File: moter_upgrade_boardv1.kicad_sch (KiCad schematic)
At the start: 41 parts, among them J10 Conn_01x03_Socket, J12 Conn_01x03_Socket, J2 USB_C_Receptacle_USB2.0_16P, J4 Conn_01x03_Socket, J5 Conn_01x02_Socket, J6 Conn_ST_STDC14, J7 Conn_01x02_Socket, J9 Conn_01x03_Socket, SW1 SW_Wuerth_450301014042, SW2 SW_Push, U1 BD33FC0FP, U2 STM32F446RETx, U3 MCP2562-E-P

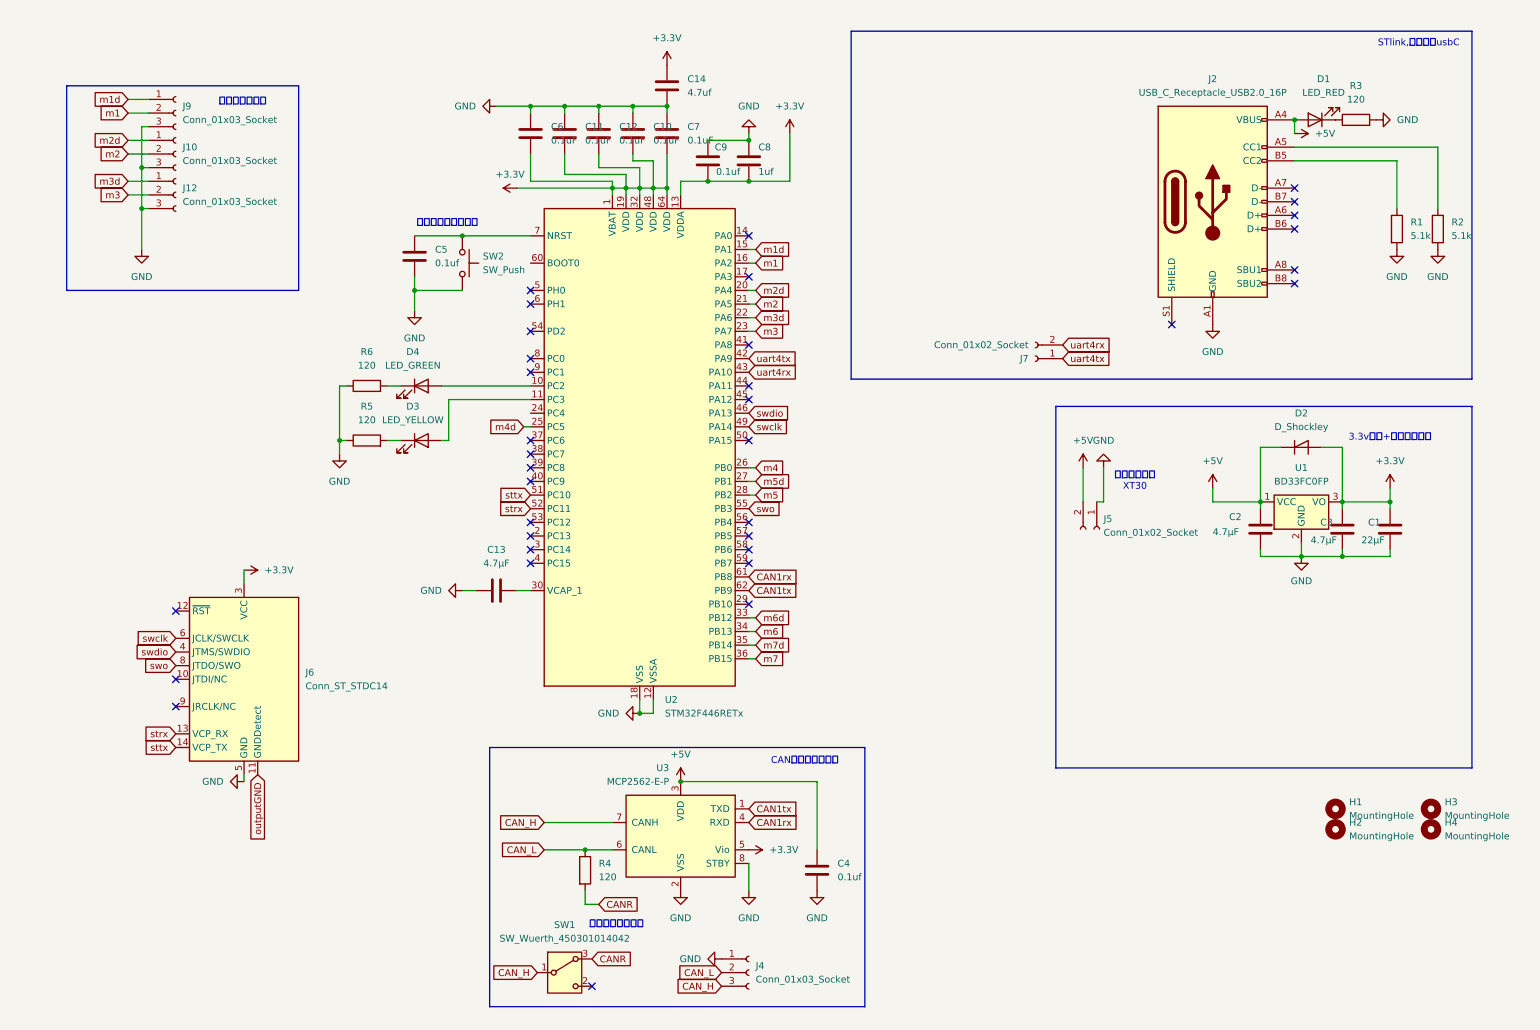
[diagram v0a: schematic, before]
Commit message: 絶縁回路の作成
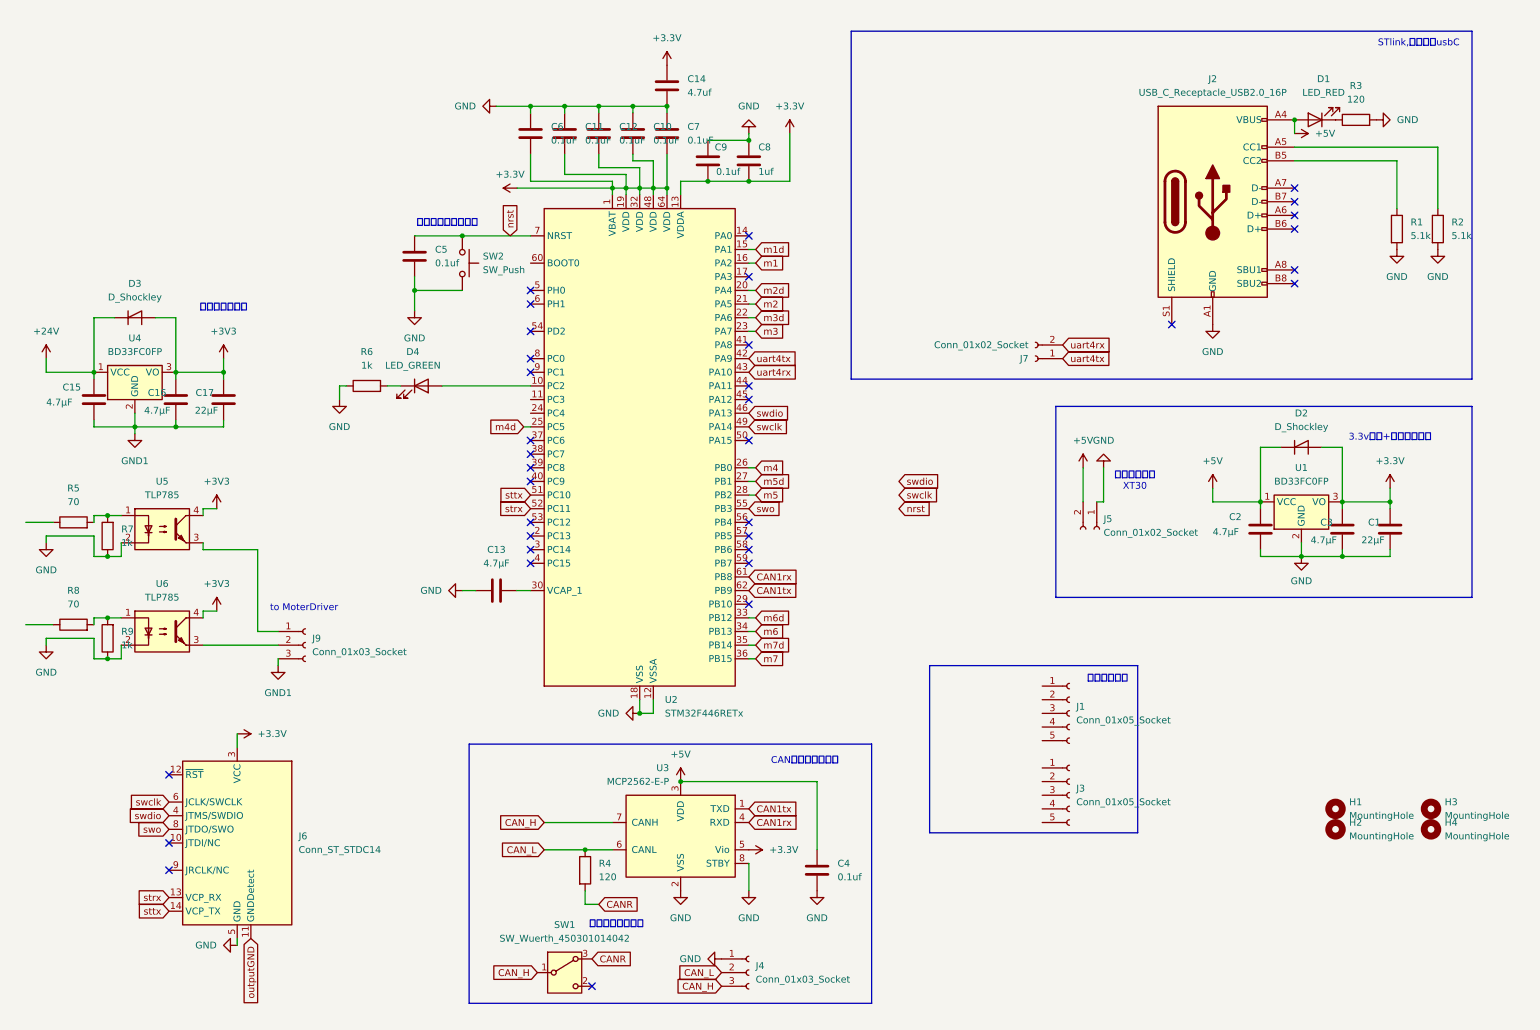
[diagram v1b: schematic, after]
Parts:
- removed D3: LED_YELLOW, Diode_SMD:D_0805_2012Metric_Pad1.15x1.40mm_HandSolder, symbol Device:LED
- removed J10, J12: Conn_01x03_Socket, Connector_JST:JST_XH_S3B-XH-A-1_1x03_P2.50mm_Horizontal, symbol Connector:Conn_01x03_Socket
- added C15, C16: 4.7μF, Capacitor_SMD:C_0805_2012Metric_Pad1.18x1.45mm_HandSolder, symbol Device:C
- added C17: 22μF, Capacitor_SMD:C_0805_2012Metric_Pad1.18x1.45mm_HandSolder, symbol Device:C
- added D3: D_Shockley, Diode_SMD:D_SOD-323_HandSoldering, symbol Device:D_Shockley
- added J1, J3: Conn_01x05_Socket, symbol Connector:Conn_01x05_Socket
- added R7, R9: 1k, Resistor_THT:R_Axial_DIN0207_L6.3mm_D2.5mm_P7.62mm_Horizontal, symbol Device:R
- added R8: 70, Resistor_THT:R_Axial_DIN0207_L6.3mm_D2.5mm_P7.62mm_Horizontal, symbol Device:R
- added U4: BD33FC0FP, Package_TO_SOT_SMD:TO-252-2, symbol Regulator_Linear:BD33FC0FP
- added U5, U6: TLP785, Package_DIP:DIP-4_W7.62mm, symbol Isolator:TLP785
- R5: value 120 -> 70; footprint Resistor_SMD:R_0603_1608Metric_Pad0.98x0.95mm_HandSolder -> Resistor_THT:R_Axial_DIN0207_L6.3mm_D2.5mm_P7.62mm_Horizontal
- R6: value 120 -> 1k
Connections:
- net GND: now also R7.1, R9.1, U5.2, U6.2; no longer J9.3 (Pin_3), R5.1
- net m1: no longer J9.2 (Pin_2)
- net m1d: no longer J9.1 (Pin_1)
- net nrst: now reaches C5.1, SW2.1, U2.7 (NRST)
- net at R5.2: now also R7.2, U5.1
- new net: R8.2, R9.2, U6.1
- new net: J9.2 (Pin_2), U6.3
- new net: J9.1 (Pin_1), U5.3
- new net +24V: C15.1, D3.1 (K), U4.1 (VCC)
- new net +3V3: C16.1, C17.1, D3.2 (A), U4.3 (VO), U5.4, U6.4
- new net GND1: C15.2, C16.2, C17.2, J9.3 (Pin_3), U4.2 (GND)
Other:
- note added: "to MoterDriver"
- note added: "エンコーダ用"
- note added: "絶縁信号の電源"
- note removed: "モーター用出力"
- moved on the sheet: J6, J9

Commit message: MCUをF446からH523へ置き換え
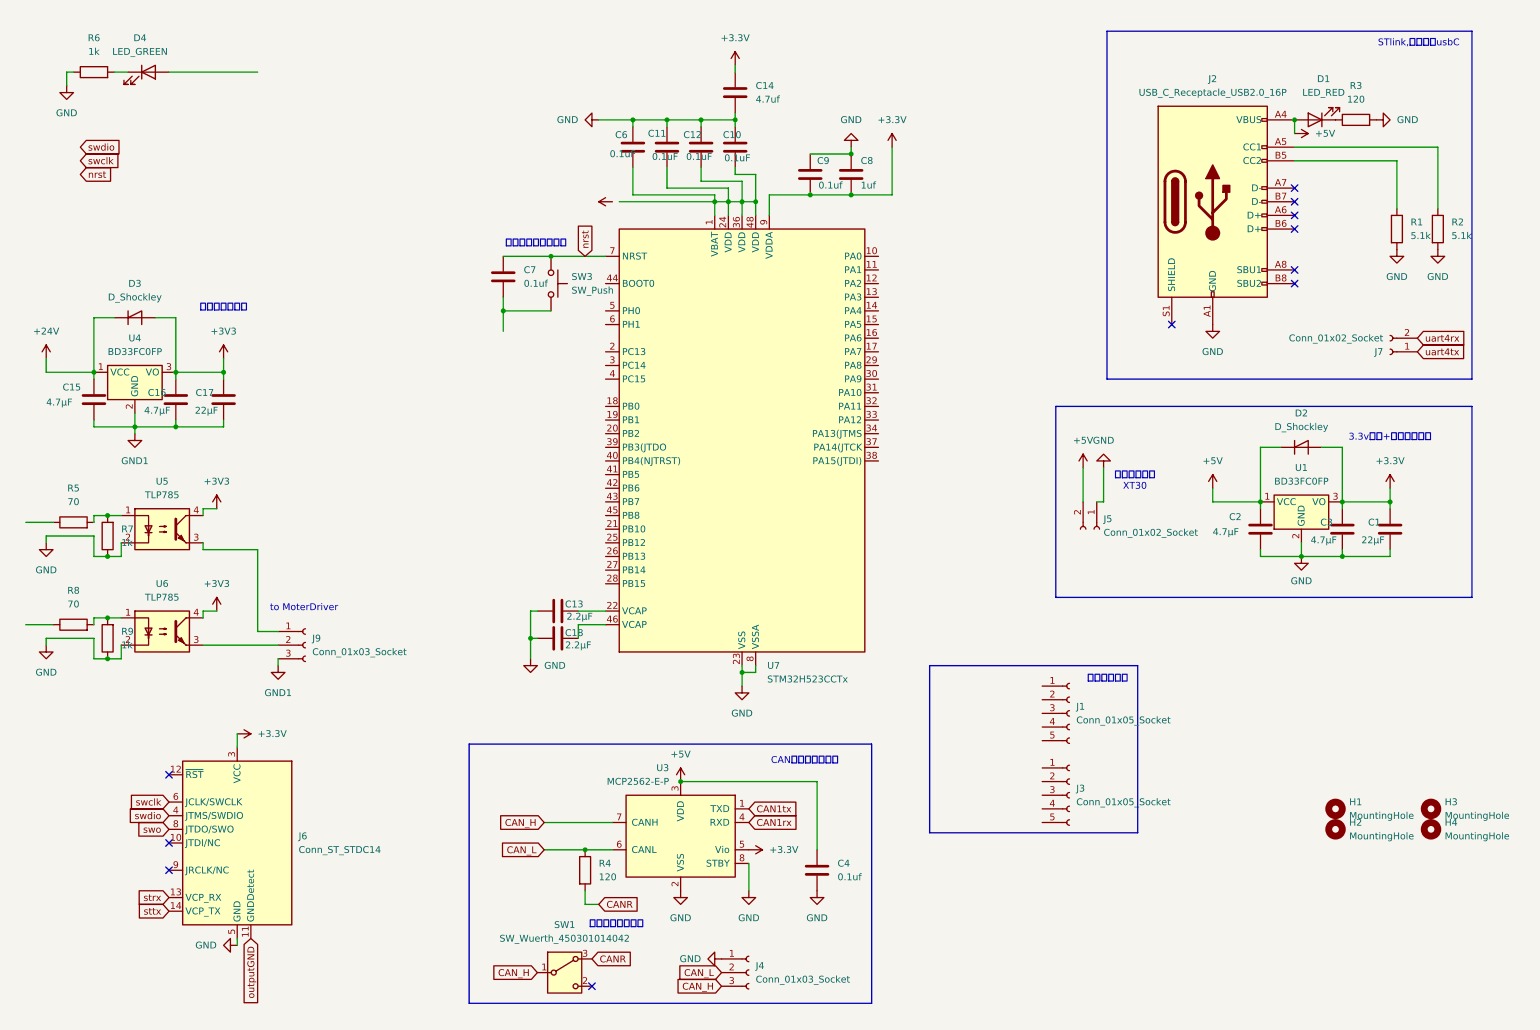
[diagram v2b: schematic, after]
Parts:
- removed C5: 0.1uf, Capacitor_SMD:C_0603_1608Metric_Pad1.08x0.95mm_HandSolder, symbol Device:C
- removed SW2: SW_Push, Button_Switch_THT:SW_PUSH_6mm, symbol Switch:SW_Push
- removed U2: STM32F446RETx, Package_QFP:LQFP-64_10x10mm_P0.5mm, symbol MCU_ST_STM32F4:STM32F446RETx
- added C18: 2.2μF, Capacitor_SMD:C_0603_1608Metric_Pad1.08x0.95mm_HandSolder, symbol Device:C
- added SW3: SW_Push, Button_Switch_THT:SW_PUSH_6mm, symbol Switch:SW_Push
- added U7: STM32H523CCTx, Package_QFP:LQFP-48_7x7mm_P0.5mm, symbol MCU_ST_STM32H5:STM32H523CCTx
- C13: value 4.7μF -> 2.2μF
- C7: value 0.1uF -> 0.1uf; footprint Capacitor_SMD:C_0402_1005Metric_Pad0.74x0.62mm_HandSolder -> Capacitor_SMD:C_0603_1608Metric_Pad1.08x0.95mm_HandSolder
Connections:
- net +3.3V: now also U7.9 (VDDA); no longer C10.1, C11.1, C12.1, C6.1, C7.1
- net GND: now also C18.1, U7.23 (VSS), U7.35 (VSS), U7.47 (VSS), U7.8 (VSSA); no longer C7.2
- net nrst: now also C7.1, SW3.1, U7.7 (NRST)
- net at C13.2: now also U7.22 (VCAP)
- new net: C10.1, C11.1, C12.1, C6.1, U7.1 (VBAT), U7.24 (VDD), U7.36 (VDD), U7.48 (VDD)
- new net: C7.2, SW3.2
- new net: C18.2, U7.46 (VCAP)
- no-connect marks 35 -> 11
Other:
- moved on the sheet: C10, C11, C12, C13, C14, C6, C8, C9, D4, J7, R6

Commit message: a
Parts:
- added J8: Conn_01x04_Socket, symbol Connector:Conn_01x04_Socket
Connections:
- net +3.3V: now also C10.1, C11.1, C12.1, C6.1, U7.1 (VBAT), U7.24 (VDD), U7.36 (VDD), U7.48 (VDD)
- net GND: now also C7.2, SW3.2, J8.2 (Pin_2)
- net nrst: now also J8.4 (Pin_4)
- net swclk: now also J8.1 (Pin_1)
- net swdio: now also J8.3 (Pin_3)
- net BOOT0: now reaches U7.44 (BOOT0)
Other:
- note added: "デバッグ用"
- moved on the sheet: C7, D4, R6, SW3

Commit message: 回路図の作図
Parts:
- removed C7: 0.1uf, Capacitor_SMD:C_0603_1608Metric_Pad1.08x0.95mm_HandSolder, symbol Device:C
- removed J3: Conn_01x05_Socket, symbol Connector:Conn_01x05_Socket
- removed J6: Conn_ST_STDC14, Connector_PinHeader_1.27mm:PinHeader_2x07_P1.27mm_Vertical, symbol Connector:Conn_ST_STDC14
- removed SW3: SW_Push, Button_Switch_THT:SW_PUSH_6mm, symbol Switch:SW_Push
- added R5: 10K, Resistor_SMD:R_0603_1608Metric_Pad0.98x0.95mm_HandSolder, symbol Device:R
- added SW1: SW_SPDT, Button_Switch_THT:SW_Slide-03_Wuerth-WS-SLTV_10x2.5x6.4_P2.54mm, symbol Switch:SW_SPDT
- added SW2: SW_Push, Button_Switch_THT:SW_PUSH_6mm, symbol Switch:SW_Push
- added U6: CH340E, Package_SO:MSOP-10_3x3mm_P0.5mm, symbol Interface_USB:CH340E
- C10, C6: footprint Capacitor_SMD:C_0402_1005Metric_Pad0.74x0.62mm_HandSolder -> Capacitor_SMD:C_0603_1608Metric_Pad1.08x0.95mm_HandSolder
- C11: renamed from C9; footprint Capacitor_SMD:C_0402_1005Metric_Pad0.74x0.62mm_HandSolder -> Capacitor_SMD:C_0603_1608Metric_Pad1.08x0.95mm_HandSolder
- C5: renamed from C18; footprint Capacitor_SMD:C_0603_1608Metric_Pad1.08x0.95mm_HandSolder -> Capacitor_SMD:C_0805_2012Metric_Pad1.18x1.45mm_HandSolder
- C7: renamed from C11; footprint Capacitor_SMD:C_0402_1005Metric_Pad0.74x0.62mm_HandSolder -> Capacitor_SMD:C_0603_1608Metric_Pad1.08x0.95mm_HandSolder
- C8: renamed from C12; footprint Capacitor_SMD:C_0402_1005Metric_Pad0.74x0.62mm_HandSolder -> Capacitor_SMD:C_0603_1608Metric_Pad1.08x0.95mm_HandSolder
- C9: renamed from C14; footprint Capacitor_SMD:C_0603_1608Metric_Pad1.08x0.95mm_HandSolder -> Capacitor_SMD:C_0805_2012Metric_Pad1.18x1.45mm_HandSolder
- D2: renamed from D4; footprint Diode_SMD:D_0805_2012Metric_Pad1.15x1.40mm_HandSolder -> Capacitor_SMD:C_0603_1608Metric_Pad1.08x0.95mm_HandSolder
- D4: renamed from D1; footprint Diode_SMD:D_0805_2012Metric_Pad1.15x1.40mm_HandSolder -> Capacitor_SMD:C_0603_1608Metric_Pad1.08x0.95mm_HandSolder
- J1: renamed from J8; footprint (none) -> Connector_JST:JST_XH_S4B-XH-A-1_1x04_P2.50mm_Horizontal
- J2: renamed from J9; footprint Connector_JST:JST_XH_S3B-XH-A-1_1x03_P2.50mm_Horizontal -> Connector_PinHeader_2.54mm:PinHeader_1x03_P2.54mm_Vertical
- J5: renamed from J1; footprint (none) -> Connector_JST:JST_XH_S5B-XH-A-1_1x05_P2.50mm_Horizontal
- R1: renamed from R5; value 70 -> 68; footprint Resistor_THT:R_Axial_DIN0207_L6.3mm_D2.5mm_P7.62mm_Horizontal -> Resistor_THT:R_Axial_DIN0207_L6.3mm_D2.5mm_P10.16mm_Horizontal
- R2: renamed from R8; value 70 -> 68; footprint Resistor_THT:R_Axial_DIN0207_L6.3mm_D2.5mm_P7.62mm_Horizontal -> Resistor_THT:R_Axial_DIN0207_L6.3mm_D2.5mm_P10.16mm_Horizontal
- R3: renamed from R7; footprint Resistor_THT:R_Axial_DIN0207_L6.3mm_D2.5mm_P7.62mm_Horizontal -> Resistor_SMD:R_0603_1608Metric_Pad0.98x0.95mm_HandSolder
- R4: renamed from R9; footprint Resistor_THT:R_Axial_DIN0207_L6.3mm_D2.5mm_P7.62mm_Horizontal -> Resistor_SMD:R_0603_1608Metric_Pad0.98x0.95mm_HandSolder
- renumbered C15 to C1, C8 to C12, C4 to C13, C2 to C14, C3 to C15, C1 to C16, C16 to C2, C17 to C3, C13 to C4, D3 to D1, D2 to D3, J4 to J3, J5 to J4, J2 to J6, R2 to R10, R4 to R6, R6 to R7, R3 to R8, R1 to R9, SW1 to SW3, U4 to U1, U5 to U2, U6 to U3, U7 to U4, U3 to U5, U1 to U7
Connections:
- net CAN1rx is gone; now on net CAN2rx: U5.4 (RXD)
- net CAN1tx is gone; now on net CAN2tx: U5.1 (TXD)
- net +3.3V: now also J5.2 (Pin_2)
- net BOOT0: now also R5.1, SW1.2 (B)
- net GND: now also J5.5 (Pin_5), R5.2, SW1.1 (A), SW2.2, U6.3 (GND)
- net nrst: now also SW2.1
- net swclk: now also U4.37 (PA14(JTCK)
- net swdio: now also U4.34 (PA13(JTMS)
- net en-b: now reaches J5.1 (Pin_1)
- net en-b: now also U4.28 (PB15)
- net en-a: now reaches J5.3 (Pin_3)
- net en-a: now also U4.27 (PB14)
- net en-x: now reaches J5.4 (Pin_4)
- net en-x: now also U4.26 (PB13)
- net at U4.11 (PA1): now also D2.2 (A)
- net wm to moter: now reaches U4.13 (PA3)
- net wm to moter: now also R2.1
- net dir to moter: now reaches U4.14 (PA4)
- net dir to moter: now also R1.1
- net CAN2rx: now reaches U4.32 (PA11)
- net CAN2tx: now reaches U4.33 (PA12)
- net uart1-tx: now reaches U4.42 (PB6)
- net uart1-rx: now reaches U4.43 (PB7)
- net d-: now reaches J6.A6 (D+)
- net d-: now also J6.B6 (D+), U6.2 (UD-)
- net d+: now reaches J6.A7 (D-)
- net d+: now also J6.B7 (D-), U6.1 (UD+)
- no-connect marks 11 -> 5
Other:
- note added: "デバッグ用 SWO"
- note removed: "デバッグ用"
- moved on the sheet: C1, C10, C11, C12, C2, C3, C4, C5, C6, C7, C8, C9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
